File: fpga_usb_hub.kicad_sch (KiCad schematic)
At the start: 143 parts, among them J11 SNAC_HDMI, J12 STX-3000, J13 DVI-I_Dual_Link, J14 DDR-SODIMM-2.5V-200, J15 Conn_01x05, J16 47018-4000, J9 Conn_QMTECH_Cyclone_V_SoC_KFB, M1 Fan_CPU_4pin, Q3 MMBT3904, SW1.RST1 1-1825027-1, SW2.OSD1 1-1825027-1, SW3.USR1 1-1825027-1, U13 PCM5102, U14 TXB0108PW, U15 TPS563240DDC, U16 MCP7940N-xST, U17 TXB0108PW, U18 TXB0108PW, U19 LM75C, U20 TXB0108PW, U21 TXB0108PW, U22 TXB0108PW, U23 TXB0108PW, U24 SN74LVC1G14DBV

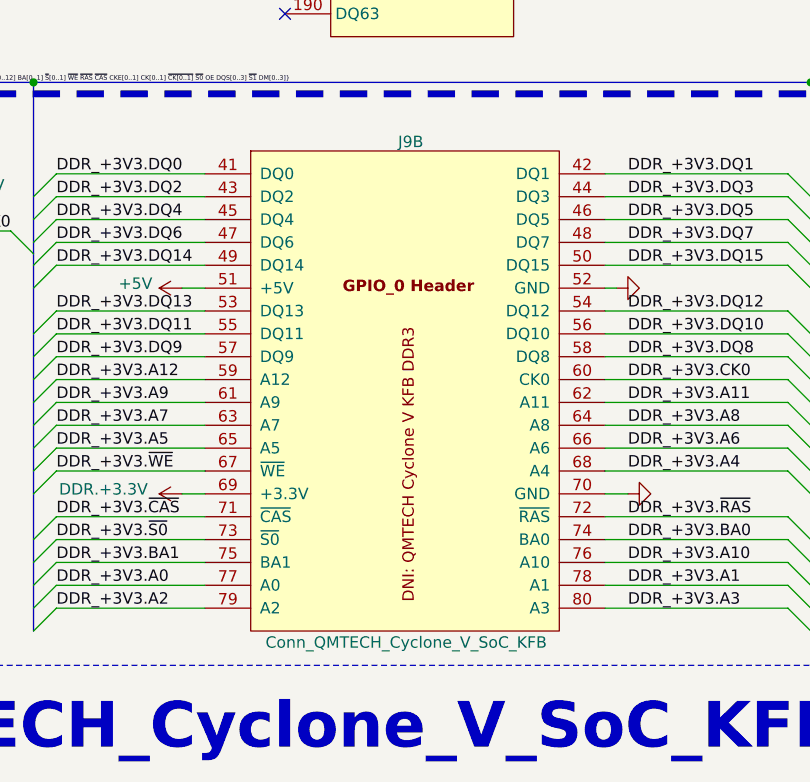
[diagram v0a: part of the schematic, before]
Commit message: BUG Fix: TCPC GPIO nets separated
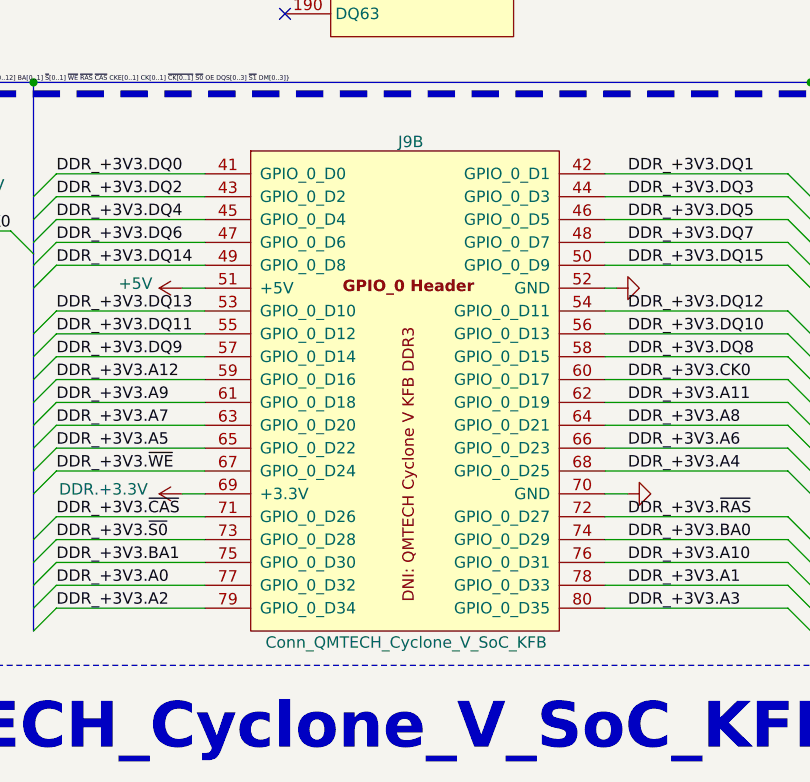
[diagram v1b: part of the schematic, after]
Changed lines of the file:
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@@
 		)
 		(pin "61"
-			(alternate "A9")
 		)
 		(pin "68"
-			(alternate "A4")
 		)
 		(pin "79"
-			(alternate "A2")
 		)
 		(pin "35"
@@
 		)
 		(pin "45"
-			(alternate "DQ4")
 		)
 		(pin "18"
@@
 		)
 		(pin "50"
-			(alternate "DQ15")
 		)
 		(pin "116"
@@
 		)
 		(pin "41"
-			(alternate "DQ0")
 		)
 		(pin "95"
 		)
 		(pin "44"
-			(alternate "DQ3")
 		)
 		(pin "63"
-			(alternate "A7")
 		)
 		(pin "19"
@@
 		)
 		(pin "56"
-			(alternate "DQ10")
 		)
 		(pin "65"
-			(alternate "A5")
 		)
 		(pin "83"
@@
 		)
 		(pin "49"
-			(alternate "DQ14")
 		)
 		(pin "38"
 		)
 		(pin "57"
-			(alternate "DQ9")
 		)
 		(pin "43"
-			(alternate "DQ2")
 		)
 		(pin "108"
@@
 		)
 		(pin "46"
-			(alternate "DQ5")
 		)
 		(pin "109"
@@
 		)
 		(pin "62"
-			(alternate "A11")
 		)
 		(pin "60"
-			(alternate "CK0")
 		)
 		(pin "110"
@@
 		)
 		(pin "47"
-			(alternate "DQ6")
 		)
 		(pin "25"
@@
 		)
 		(pin "80"
-			(alternate "A3")
 		)
 		(pin "9"
@@
 		)
 		(pin "59"
-			(alternate "A12")
 		)
 		(pin "32"
@@
 		)
 		(pin "64"
-			(alternate "A8")
 		)
 		(pin "58"
-			(alternate "DQ8")
 		)
 		(pin "23"
@@
 		)
 		(pin "73"
-			(alternate "~{S0}")
 		)
 		(pin "42"
-			(alternate "DQ1")
 		)
 		(pin "53"
-			(alternate "DQ13")
 		)
 		(pin "89"
@@
 		)
 		(pin "77"
-			(alternate "A0")
 		)
 		(pin "54"
-			(alternate "DQ12")
 		)
 		(pin "14"
@@
 		)
 		(pin "48"
-			(alternate "DQ7")
 		)
 		(pin "75"
-			(alternate "BA1")
 		)
 		(pin "37"
@@
 		)
 		(pin "78"
-			(alternate "A1")
 		)
 		(pin "29"
@@
 		)
 		(pin "55"
-			(alternate "DQ11")
 		)
 		(pin "2"
@@
 		)
 		(pin "72"
-			(alternate "~{RAS}")
 		)
 		(pin "120"
 		)
 		(pin "66"
-			(alternate "A6")
 		)
 		(pin "52"
@@
 		)
 		(pin "67"
-			(alternate "~{WE}")
 		)
 		(pin "16"
@@
 		)
 		(pin "76"
-			(alternate "A10")
 		)
 		(pin "1"
 		)
 		(pin "74"
-			(alternate "BA0")
 		)
 		(pin "88"
 		)
 		(pin "71"
-			(alternate "~{CAS}")
 		)
 		(pin "104"

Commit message: Cleared the annotation and regenerated PDF schematic
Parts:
- renumbered BT1 to BT?, C103 to C?, C95 to C?, C75 to C?, C107 to C?, C70 to C?, C85 to C?, C102 to C?, C106 to C?, C104 to C?, C96 to C?, C105 to C?, C109 to C?, C98 to C?, C66 to C?, C74 to C?, C110 to C?, C82 to C?, C90 to C?, C84 to C?, C69 to C?, C86 to C?, C64 to C?, C72 to C?, C114 to C?, C68 to C?, C87 to C?, C111 to C?, C78 to C?, C81 to C?, C80 to C?, C89 to C?, C83 to C?, C97 to C?, C79 to C?, C92 to C?, C108 to C?, C100 to C?, C67 to C?, C113 to C?, C99 to C?, C76 to C?, C94 to C?, C93 to C?, C91 to C?, C73 to C?, C63 to C?, C77 to C?, C101 to C?, C65 to C?, C112 to C?, C71 to C?, C88 to C?, D1 to D?, J9 to J?, J15 to J?, J13 to J?, J11 to J?, J14 to J?, J16 to J?, J12 to J?, JP24 to JP?, JP23 to JP?, JP22 to JP?, JP21 to JP?, JP20 to JP?, L3 to L?, M1 to M?, Q3 to Q?, R88 to R?, R35 to R?, R85 to R?, R54 to R?, R59 to R?, R66 to R?, R40 to R?, R41 to R?, R53 to R?, R79 to R?, R37 to R?, R72 to R?, R34 to R?, R89 to R?, R86 to R?, R69 to R?, R75 to R?, R46 to R?, R50 to R?, R44 to R?, R64 to R?, R48 to R?, R68 to R?, R82 to R?, R36 to R?, R52 to R?, R56 to R?, R58 to R?, R81 to R?, R55 to R?, R39 to R?, R51 to R?, R65 to R?, R57 to R?, R43 to R?, R77 to R?, R67 to R?, R78 to R?, R42 to R?, R61 to R?, R62 to R?, R84 to R?, R47 to R?, R38 to R?, R45 to R?, R74 to R?, R49 to R?, R83 to R?, R90 to R?, R76 to R?, R87 to R?, R91 to R?, R71 to R?, R70 to R?, R60 to R?, R63 to R?, R73 to R?, R80 to R?, SW1.RST1 to SW1.RST?, SW2.OSD1 to SW2.OSD?, SW3.USR1 to SW3.USR?, U22 to U?, U23 to U?, U15 to U?, U14 to U?, U21 to U?, U17 to U?, U19 to U?, U20 to U?, U16 to U?, U24 to U?, U18 to U?, U13 to U?, XTAL1 to XTAL?
